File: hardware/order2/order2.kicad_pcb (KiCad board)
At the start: 2 copper layers, 137 x 65 mm, 99 parts, among them IC1 ATMEGA88A-A, J1 RJ45_8P8C_8FACH, K1 pow_sel, P1 UART, P2 Shield, P3 i2c_pow, P4 i2c_chain, P5 12Vin, P6 HOHLBUCHSE, P7 Vccin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

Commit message: order2_s2
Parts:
- added C1: 100nF, SM0603_big, F.Cu at (79.1, 44.0)
- added C1: 100nF, SM0603_big, F.Cu at (60.5, 71.2)
- added C2: 10uF, SM0805_big, F.Cu at (92.0, 29.0)
- added C2: 100nF, SM0603_big, F.Cu at (69.2, 56.8)
- added C3: 100nF, SM0603_big, F.Cu at (95.2, 42.0)
- added C3: 10uF, SM0805_big, F.Cu at (72.8, 56.8)
- added C4: 10uF, SM0805_big, F.Cu at (95.0, 29.0)
- added C4: 100nF, SM0603_big, F.Cu at (80.0, 62.2)
- added C5: 100nF, SM0603_big, F.Cu at (100.5, 35.5)
- added C6: 100nF, SM0603_big, F.Cu at (62.5, 43.5)
- added D1: LED, SM0603_big, F.Cu at (72.4, 30.0)
- added D2: LED, SM0603_big, F.Cu at (72.4, 27.6)
- added IC1: ATMEGA88-A, TQFP32, F.Cu at (74.0, 38.0)
- added J1: RJ45, RJ45_8P8_simple, F.Cu at (113.0, 36.0)
- added J1: RJ45, RJ45_8P8_simple, F.Cu at (86.0, 64.0)
- added P1: ISP, wannenstecker_2x5_rm254, F.Cu at (85.0, 36.0)
- added P2: UART, Stiftleiste_4x1, F.Cu at (64.6, 41.8)
- added R1: 150, SM0805_big, F.Cu at (77.0, 30.0)
- added R1: 220, SM0603_big, F.Cu at (64.5, 71.2)
- added R2: 150, SM0805_big, F.Cu at (77.0, 27.6)
- added R2: 22k, SM0603_big, F.Cu at (76.2, 61.5)
- added R3: 10k, SM0603_big, F.Cu at (91.7, 42.0)
- added R3: 22k, SM0603_big, F.Cu at (76.2, 56.5)
- added R4: 22k, SM0603_big, F.Cu at (98.2, 42.0)
- added R4: 120, SM0603_big, F.Cu at (80.0, 58.2)
- added R5: 22k, SM0603_big, F.Cu at (98.0, 29.0)
- added R6: 120, SM0603_big, F.Cu at (100.5, 31.5)
- added SW1: SW_RESET, Taster_6mm, F.Cu at (106.5, 30.0)
- added U1: ST485, st485, F.Cu at (96.0, 36.0)
- added U1: TSIC50XF, Tsic_TO92, F.Cu at (29.5, 64.0)
- added U2: HYT271, HYT271, F.Cu at (29.5, 36.0)
- added U2: ST485, st485, F.Cu at (70.2, 64.0)
- added m3_loch: VAL**, m3_loch, F.Cu at (105.5, 41.0)
- added m3_loch: VAL**, m3_loch, F.Cu at (64.0, 31.0)
- added m3_loch: VAL**, m3_loch, F.Cu at (77.8, 69.0)
- added m3_loch: VAL**, m3_loch, F.Cu at (61.8, 59.0)
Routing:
- net GND: track 883.2 -> 1194.5 mm, vias 3 -> 10
- net VCC: track 556.5 -> 806.0 mm, vias 3 -> 8
- net /RESET: track 106.9 -> 162.7 mm, vias 2 -> 4
- net /za: track 0.00 -> 53.3 mm, vias 0 -> 1
- net /zb: track 0.00 -> 52.6 mm
- net N-000007: track 3.76 -> 49.3 mm
- net /SDA: track 81.2 -> 122.1 mm
- net /SCL: track 89.2 -> 129.1 mm
- net N-0000010: track 0.00 -> 39.5 mm
- net /DI: track 0.00 -> 18.5 mm
- net /MOSI: track 49.6 -> 61.4 mm, vias 2 -> 3
- net /SCK: track 11.9 -> 22.5 mm
- net /RX: track 46.4 -> 56.4 mm
- net /MISO: track 8.73 -> 18.5 mm
- net /LED2: track 17.8 -> 24.9 mm
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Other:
- board size 137 x 65 mm -> 137 x 159 mm
- rule trace_min: 0.4 -> 0.254

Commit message: order2_s3
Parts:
- added D1: LED, SM0603_big, F.Cu at (241.0, 157.5)
- added P1: CONN_8, Stiftleiste_8x1, F.Cu at (208.7, 119.2)
- added P10: CONN_10, Stiftleiste_10x1, F.Cu at (263.0, 111.5)
- added P11: CONN_8, Stiftleiste_8x1, F.Cu at (263.0, 137.0)
- added P2: CONN_6, Stiftleiste_6x1, F.Cu at (208.7, 139.5)
- added P3: CONN_6, Stiftleiste_6x1, B.Cu at (211.7, 139.5)
- added P4: CONN_8, Stiftleiste_8x1, B.Cu at (211.7, 119.2)
- added P5: POW, Stiftleiste_2x1, F.Cu at (236.0, 158.5)
- added P6: TWI, wannenstecker_2x3_rm254, F.Cu at (250.5, 157.0)
- added P7: TWI_POW, wannenstecker_2x3_rm254, F.Cu at (221.0, 157.0)
- added P8: CONN_10, Stiftleiste_10x1, B.Cu at (260.0, 112.5)
- added P9: CONN_8, Stiftleiste_8x1, B.Cu at (260.0, 137.0)
- added R1: 150, SM0805_big, F.Cu at (240.0, 154.0)
- added R2: 2k2, SM0603_big, F.Cu at (230.5, 154.5)
- added R3: 2k2, SM0603_big, F.Cu at (233.0, 154.5)
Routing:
- net GND: track 1194.5 -> 1362.8 mm, vias 10 -> 12
- net /SDA: track 122.1 -> 231.7 mm
- net /SCL: track 129.1 -> 234.9 mm, vias 2 -> 4
- net VCC: track 806.0 -> 903.0 mm
- net /LED: track 0.00 -> 38.7 mm, vias 0 -> 1
- net N-0000033: track 0.00 -> 3.98 mm
- net N-0000012: track 0.00 -> 3.42 mm
- net N-0000010: track 39.5 -> 42.9 mm
- net N-000009: track 0.00 -> 3.42 mm
- net N-000008: track 3.76 -> 7.18 mm
- net N-0000014: track 2.11 -> 5.53 mm
- net N-0000013: track 0.00 -> 3.42 mm
- net N-0000011: track 0.00 -> 3.42 mm
- net N-000007: track 49.3 -> 52.3 mm
- net N-000006: track 0.00 -> 3.00 mm
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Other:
- board size 137 x 159 mm -> 246 x 159 mm
- net class uc removed

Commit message: s4
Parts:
- moved P8 50.6 mm to (214.0, 133.5)
- moved D1 50.6 mm to (195.0, 178.5)
- moved P1 50.6 mm to (162.7, 140.2)
- moved P10 50.6 mm to (217.0, 132.5)
- moved P11 50.6 mm to (217.0, 158.0)
- moved P2 50.6 mm to (162.7, 160.5)
- moved P3 50.6 mm to (165.7, 160.5)
- moved P4 50.6 mm to (165.7, 140.2)
- moved P5 50.6 mm to (190.0, 179.5)
- moved P6 50.6 mm to (204.5, 178.0)
- moved P7 50.6 mm to (175.0, 178.0)
- moved P9 50.6 mm to (214.0, 158.0)
- moved R1 50.6 mm to (194.0, 175.0)
- moved R2 50.6 mm to (184.5, 175.5)
- moved R3 50.6 mm to (187.0, 175.5)
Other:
- board size 246 x 159 mm -> 200 x 159 mm

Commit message: s5
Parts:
- added P1: CONN_4, Stiftleiste_4x1, F.Cu at (284.2, 57.2)
- added P2: so8, st485, F.Cu at (288.6, 57.2)
- added P3: CONN_4, Stiftleiste_4x1, F.Cu at (296.9, 57.2)
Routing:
- net N-000008: track 7.18 -> 11.8 mm
- net N-000004: track 3.00 -> 7.58 mm
- net N-000002: track 3.00 -> 7.42 mm
- net N-000006: track 3.00 -> 7.31 mm
- net N-000001: track 3.00 -> 6.52 mm
- net N-000005: track 3.00 -> 6.52 mm
- net N-000003: track 5.11 -> 8.52 mm
- net N-000007: track 52.3 -> 55.7 mm
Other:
- board size 200 x 159 mm -> 278.4 x 159 mm
- net class Default: trace_width 0.7 -> 0.6; via_dia 1.2 -> 0.889; via_drill 0.6 -> 0.635
- board text added: "SO8"

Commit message: s6
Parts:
- added P1: CONN_4, Stiftleiste_4x1, F.Cu at (303.7, 65.3)
- added P2: so8, st485, F.Cu at (303.7, 60.9)
- added P3: CONN_4, Stiftleiste_4x1, F.Cu at (303.7, 52.6)
- moved P1 10.2 mm to (288.7, 66.3), turned to 180 degrees
- moved P3 8.94 mm to (288.7, 53.6), turned to 180 degrees
- moved P2 4.71 mm to (288.7, 61.9), turned to 180 degrees
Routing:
- net N-000008: track 11.8 -> 16.4 mm
- net N-000004: track 7.58 -> 12.2 mm
- net N-000002: track 7.42 -> 11.8 mm
- net N-000006: track 7.31 -> 11.6 mm
- net N-000001: track 6.52 -> 10.0 mm
- net N-000005: track 6.52 -> 10.0 mm
- net N-000003: track 8.52 -> 11.9 mm
- net N-000007: track 55.7 -> 59.1 mm
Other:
- board size 278.4 x 159 mm -> 289 x 159 mm

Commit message: s7
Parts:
- added K1: CONN_3, Stiftleiste_3x1, F.Cu at (295.7, 99.5)
- added K2: CONN_3, Tsic_TO92, F.Cu at (290.6, 99.5)
- added P1: CONN_4, HYT271, F.Cu at (316.2, 96.3)
- added P2: CONN_4, Stiftleiste_4x1, F.Cu at (321.3, 96.3)
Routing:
- net N-000001: track 10.0 -> 23.6 mm
- net N-000003: track 11.9 -> 24.9 mm
- net N-000002: track 11.8 -> 24.3 mm
- net N-000004: track 12.2 -> 18.1 mm
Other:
- board size 289 x 159 mm -> 302.8 x 159 mm

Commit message: all boards
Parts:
- moved U2 330.7 mm to (294.0, 234.5), turned to 0 degrees
- moved C6 286.5 mm to (301.5, 201.5), turned to 240 degrees
- moved P2 283.1 mm to (299.8, 199.4), turned to 60 degrees
- moved m3_loch 281.4 mm to (289.0, 200.0), turned to 90 degrees
- moved D1 269.4 mm to (288.0, 191.6), turned to 270 degrees
- moved IC1 269.1 mm to (296.0, 190.0), turned to 180 degrees
- moved D2 269.0 mm to (285.6, 191.6), turned to 270 degrees
- moved C1 263.7 mm to (302.0, 184.9), turned to 180 degrees
- moved R1 263.0 mm to (288.0, 187.0), turned to 90 degrees
- moved R2 262.5 mm to (285.6, 187.0), turned to 90 degrees
- moved P1 253.2 mm to (294.0, 179.0), turned to 0 degrees
- moved R3 245.7 mm to (300.0, 172.3), turned to 0 degrees
- moved C2 241.8 mm to (287.0, 172.0), turned to 0 degrees
- moved C3 240.8 mm to (300.0, 168.8), turned to 180 degrees
- moved U1 238.0 mm to (294.0, 168.0), turned to 0 degrees
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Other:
- board size 302.8 x 159 mm -> 302.8 x 198.9 mm

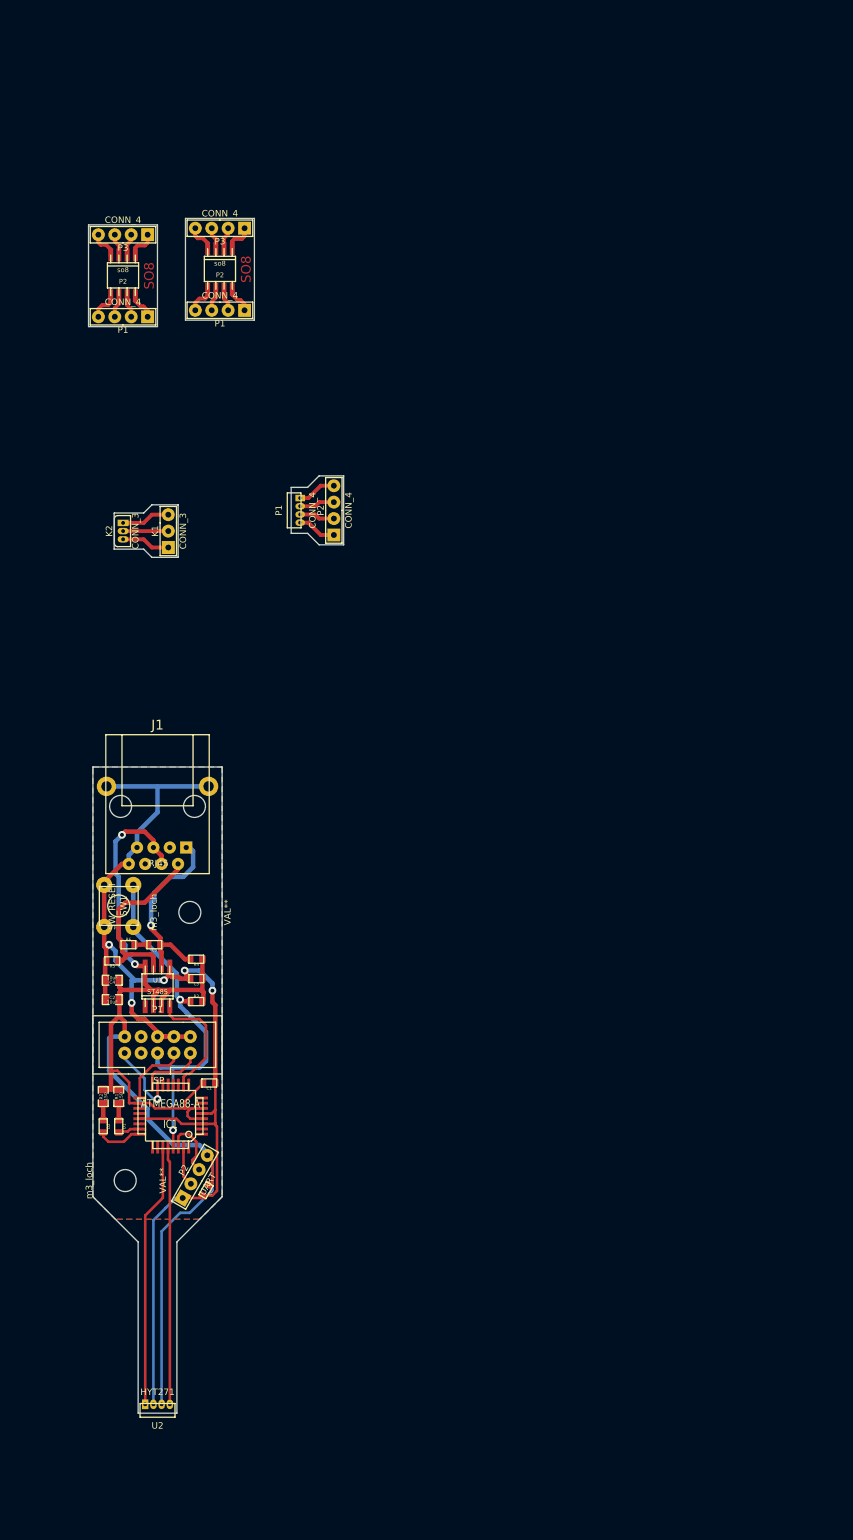
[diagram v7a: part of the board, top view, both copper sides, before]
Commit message: 2 humidity together
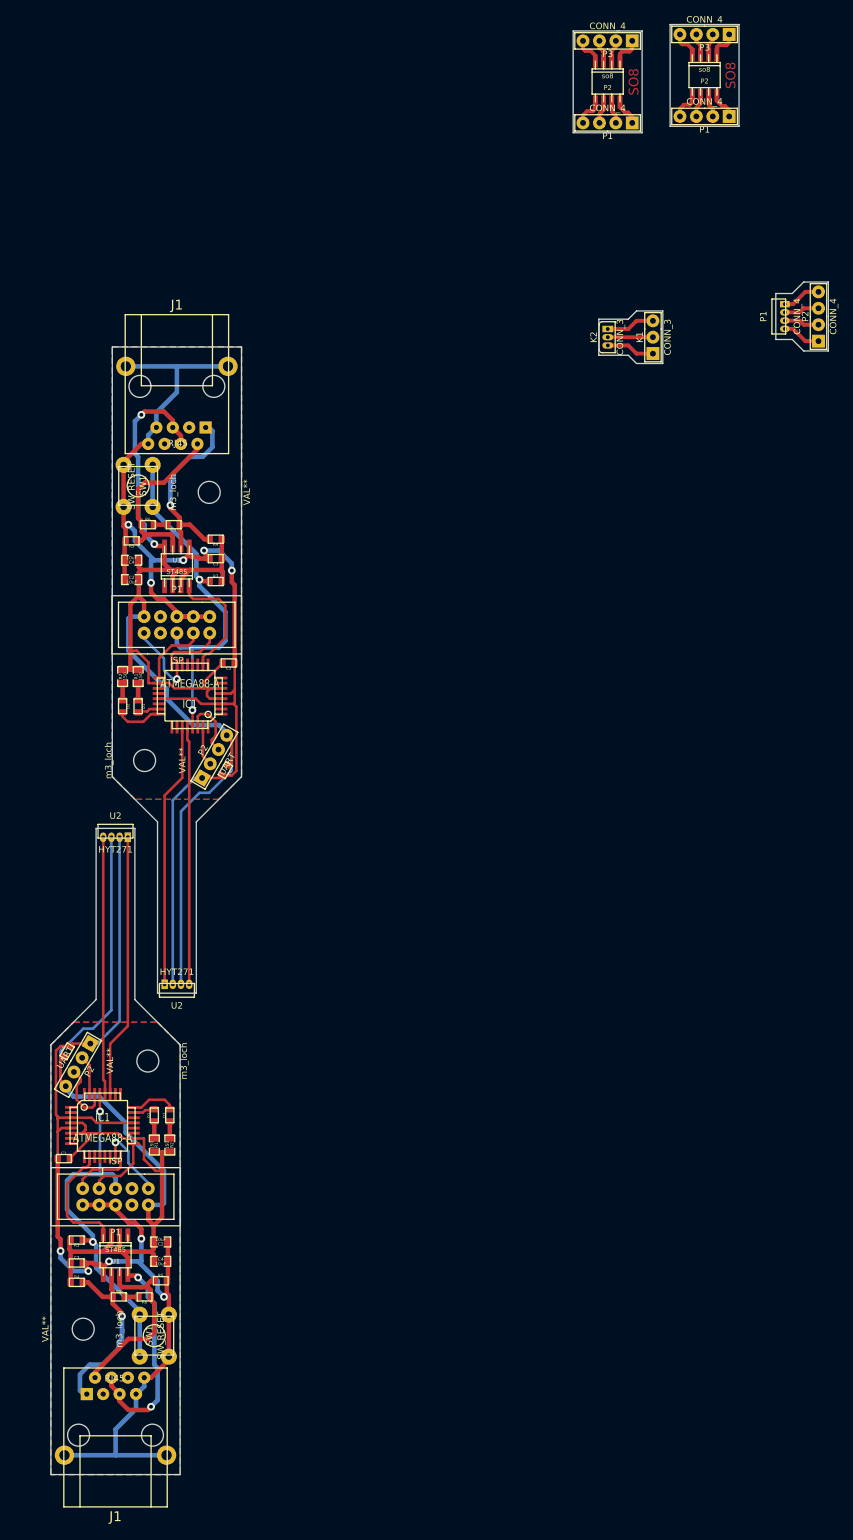
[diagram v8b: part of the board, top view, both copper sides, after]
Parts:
- added C1: 100nF, SM0603_big, F.Cu at (279.5, 196.6)
- added C2: 10uF, SM0805_big, F.Cu at (294.5, 209.5)
- added C3: 100nF, SM0603_big, F.Cu at (281.5, 212.8)
- added C4: 10uF, SM0805_big, F.Cu at (294.5, 212.5)
- added C5: 100nF, SM0603_big, F.Cu at (288.0, 218.0)
- added C6: 100nF, SM0603_big, F.Cu at (280.0, 180.0)
- added D1: LED, SM0603_big, F.Cu at (293.5, 189.9)
- added D2: LED, SM0603_big, F.Cu at (295.9, 189.9)
- added IC1: ATMEGA88-A, TQFP32, F.Cu at (285.5, 191.5)
- added J1: RJ45, RJ45_8P8_simple, F.Cu at (287.5, 230.5)
- added P1: ISP, wannenstecker_2x5_rm254, F.Cu at (287.5, 202.5)
- added P2: UART, Stiftleiste_4x1, F.Cu at (281.7, 182.1)
- added R1: 150, SM0805_big, F.Cu at (293.5, 194.5)
- added R2: 150, SM0805_big, F.Cu at (295.9, 194.5)
- added R3: 10k, SM0603_big, F.Cu at (281.5, 209.2)
- added R4: 22k, SM0603_big, F.Cu at (281.5, 215.8)
- added R5: 22k, SM0603_big, F.Cu at (294.5, 215.5)
- added R6: 120, SM0603_big, F.Cu at (292.0, 218.0)
- added SW1: SW_RESET, Taster_6mm, F.Cu at (293.5, 224.0)
- added U1: ST485, st485, F.Cu at (287.5, 213.5)
- added U2: HYT271, HYT271, F.Cu at (287.5, 147.0)
- added m3_loch: VAL**, m3_loch, F.Cu at (292.5, 181.5)
- added m3_loch: VAL**, m3_loch, F.Cu at (282.5, 223.0)
- moved K1 80.8 mm to (370.7, 69.5)
- moved K2 80.8 mm to (365.6, 69.5)
- moved P1 80.8 mm to (391.2, 66.3)
- moved P2 80.8 mm to (396.3, 66.3)
- moved P1 80.8 mm to (378.7, 35.3)
- moved P1 80.8 mm to (363.7, 36.3)
- moved P2 80.8 mm to (378.7, 30.9)
- moved P2 80.8 mm to (363.7, 31.9)
- moved P3 80.8 mm to (378.7, 22.6)
- moved P3 80.8 mm to (363.7, 23.6)
- moved R3 65.1 mm to (303.0, 107.3)
- moved C1 65.1 mm to (305.0, 119.9)
- moved C2 65.1 mm to (290.0, 107.0)
- moved C3 65.1 mm to (303.0, 103.8)
- moved C4 65.1 mm to (290.0, 104.0)
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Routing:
- net VCC: track 903.0 -> 1094.8 mm, vias 8 -> 10
- net GND: track 1362.8 -> 1547.1 mm, vias 12 -> 17
- net /RESET: track 162.7 -> 218.5 mm, vias 4 -> 6
- net /SDA: track 231.7 -> 272.6 mm
- net /SCL: track 234.9 -> 274.8 mm
- net /za: track 53.3 -> 82.4 mm, vias 1 -> 2
- net /zb: track 52.6 -> 80.3 mm
- net /DI: track 18.5 -> 37.0 mm
- net /MOSI: track 61.4 -> 73.2 mm, vias 3 -> 4
- net /SCK: track 22.5 -> 33.2 mm
- net /RX: track 56.4 -> 66.5 mm
- net /MISO: track 18.5 -> 28.2 mm
- net /LED2: track 24.9 -> 32.0 mm
- net /TX: track 54.7 -> 60.8 mm
- net /LED1: track 17.1 -> 20.6 mm
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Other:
- board size 302.8 x 198.9 mm -> 377.8 x 228.9 mm
